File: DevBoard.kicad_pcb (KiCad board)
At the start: 2 copper layers, 100 x 100 mm, 116 parts, among them J1 Audio_In, J10 Jumper, J11 RJ45, J12 Jumper, J13 Jumper, J14 Jumper, J15 Jumper, J16 Jumper, J17 Jumper, J18 DAC_I2S, J19 DAC_OUT, J2 Audio_In, J20 DAC_Amplified, J21 DAC_Amplified, J22 Voltmeter_Power, J23 Voltmeter_Positive, J24 Voltmeter_Ground, J25 Conn_01x05_Pin, J26 Pot1, J27 Pot2, J28 Pot3, J29 Pot4, J3 Audio_Amplified, J30 CV_In, J31 Audio12V_In, J32 Audio_Scaled_Out, J33 CV_Scaled_Out, J4 Audio_Amplified, J5 CV_In, J6 CV_In, J7 CV_Amplified, J8 CV_Amplified, J9 Jumper, SW1 SW_DPST, U1 MCP6004, U2 TL074, U3 LM1117-3.3, U4 LM1117-5.0, U5 LM4040DBZ-5, U6 PCM5100APW, U8 TL072

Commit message: Started PCB layout
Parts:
- J11: moved to B.Cu
- moved R14 258.4 mm to (185.6, 105.4)
- moved R16 256.6 mm to (185.6, 101.4)
- moved R20 253.9 mm to (185.6, 107.4)
- moved R18 252.8 mm to (185.6, 95.4)
- moved R22 251.3 mm to (185.6, 97.4), turned to 180 degrees
- moved R24 250.5 mm to (185.6, 109.4)
- moved J3 247.0 mm to (185.4, 85.4), turned to -90 degrees
- moved R26 246.8 mm to (185.6, 93.4)
- moved R13 244.1 mm to (170.4, 105.4), turned to 180 degrees
- moved J4 243.1 mm to (185.4, 89.6), turned to -90 degrees
- moved R15 242.1 mm to (170.4, 101.4), turned to 180 degrees
- moved J1 241.6 mm to (170.6, 85.4), turned to 90 degrees
- moved R17 240.3 mm to (170.4, 95.4), turned to 180 degrees
- moved R19 239.6 mm to (170.4, 107.4), turned to 180 degrees
- moved J2 237.7 mm to (170.6, 89.6), turned to 90 degrees
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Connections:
- C6 pad 1: Net-(U2B-+) -> Net-(U2D-+)
- J1 pad 2: /Audio_In2 -> /Audio_Out1
- J2 pad 2: /Audio_In2 -> /Audio_Out1
- J3 pad 1: /Audio_Out1 -> /Audio_In2
- J30 pad 1: /CV_In2 -> /CV_In1
- J30 pad 2: /CV_In1 -> /CV_Scaled1
- J31 pad 2: /Audio12V_In2 -> /Audio_Scaled1
- J32 pad 1: /Audio_Scaled1 -> /Audio12V_In2
- J33 pad 1: /CV_Scaled1 -> /CV_In2
- J4 pad 1: /Audio_Out1 -> /Audio_In2
- J5 pad 2: /CV2_In -> /CV1_Out
- J6 pad 2: /CV2_In -> /CV1_Out
- J7 pad 1: /CV1_Out -> /CV2_In
- J8 pad 1: /CV1_Out -> /CV2_In
- R13 pad 1: Net-(U2C--) -> Net-(U2B--)
- R14 pad 1: Net-(U2D--) -> Net-(U2C--)
- R16 pad 1: Net-(U2B-+) -> Net-(U2D-+)
- R18 pad 1: Net-(U2B--) -> Net-(U2D--)
- R19 pad 2: Net-(U2C--) -> Net-(U2B--)
- R20 pad 2: Net-(U2D--) -> Net-(U2C--)
- R22 pad 2: Net-(U2B--) -> Net-(U2D--)
- U2 pad 10: /CV1_In -> /CV2_In
- U2 pad 12: /CV2_In -> Net-(U2D-+)
- U2 pad 14: Net-(R20-Pad1) -> Net-(R22-Pad1)
- U2 pad 5: Net-(U2B-+) -> /CV1_In
- U2 pad 7: Net-(R22-Pad1) -> Net-(R19-Pad1)
- U2 pad 8: Net-(R19-Pad1) -> Net-(R20-Pad1)
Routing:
- net /CV_Scaled2: track 5.94 -> 28.6 mm
- net /Audio_Scaled2: track 5.51 -> 26.8 mm
- net /CV1_In: track 0.00 -> 17.7 mm
- net /CV2_In: track 0.00 -> 17.4 mm
- net /Audio_In2: track 0.00 -> 16.7 mm
- net /Audio_In1: track 0.00 -> 16.7 mm
- net /Audio_Scaled1: track 5.59 -> 19.6 mm
- net Net-(R22-Pad1): track 0.00 -> 13.1 mm
- net /DAC_OUT_L: track 0.00 -> 13.0 mm
- net Net-(R21-Pad1): track 0.00 -> 12.8 mm
- net /Audio_Out2: track 0.00 -> 9.51 mm
- net /Audio_Out1: track 0.00 -> 9.51 mm
- net +12V: track 0.00 -> 9.40 mm
- net +3.3VA: track 0.00 -> 9.35 mm
- net Net-(U8B--): track 0.00 -> 8.65 mm
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
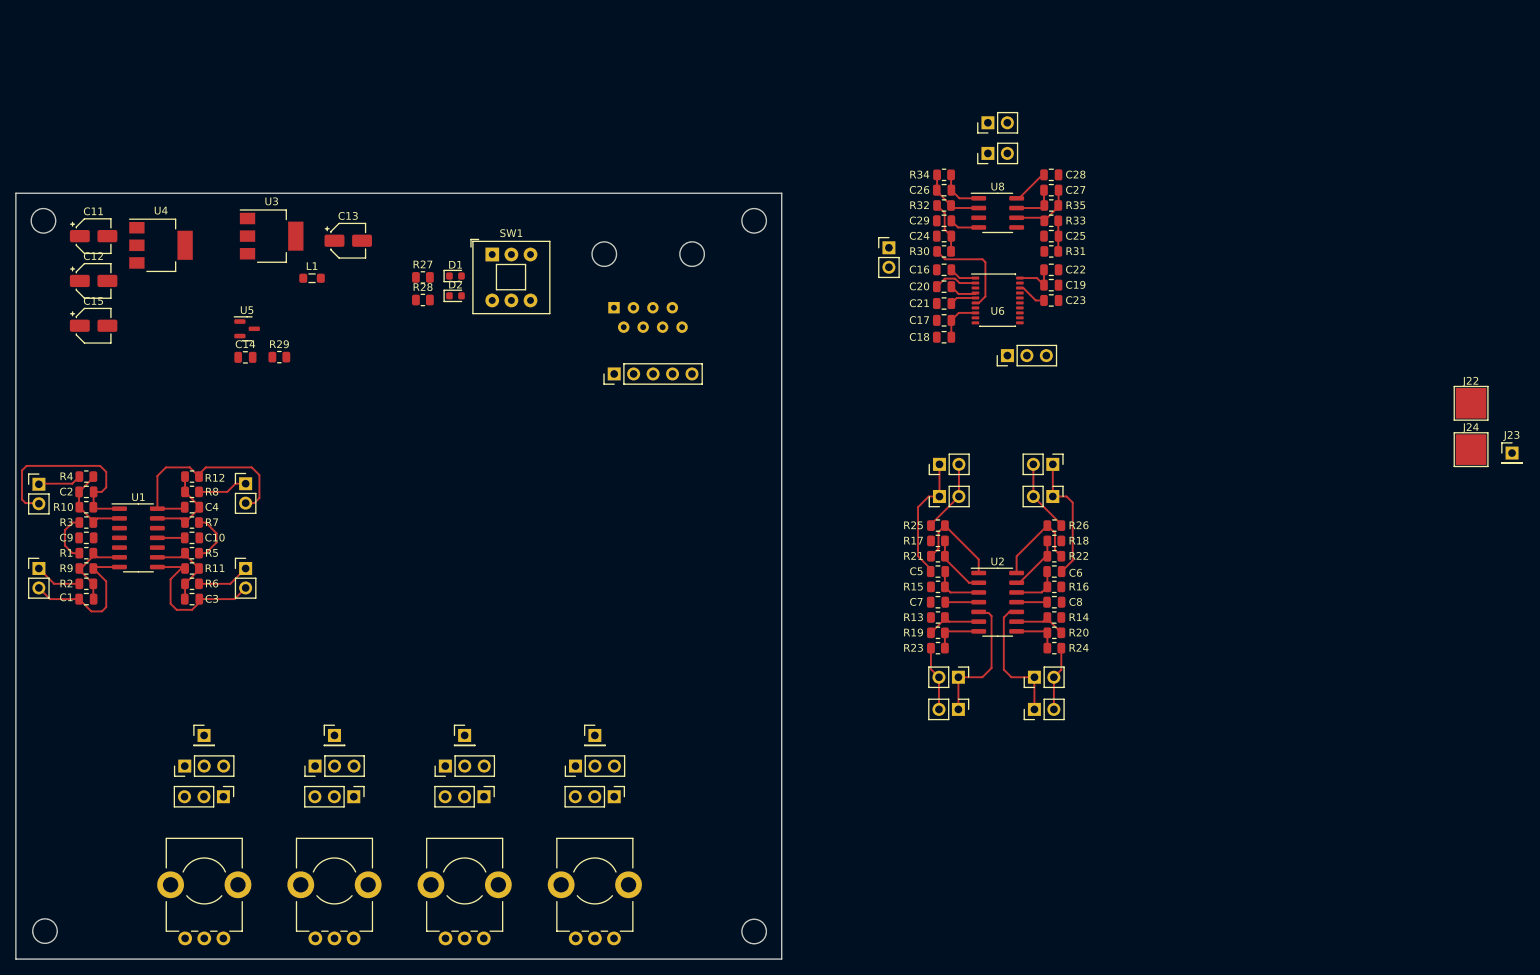
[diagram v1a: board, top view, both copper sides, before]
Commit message: Routing scaling circuits
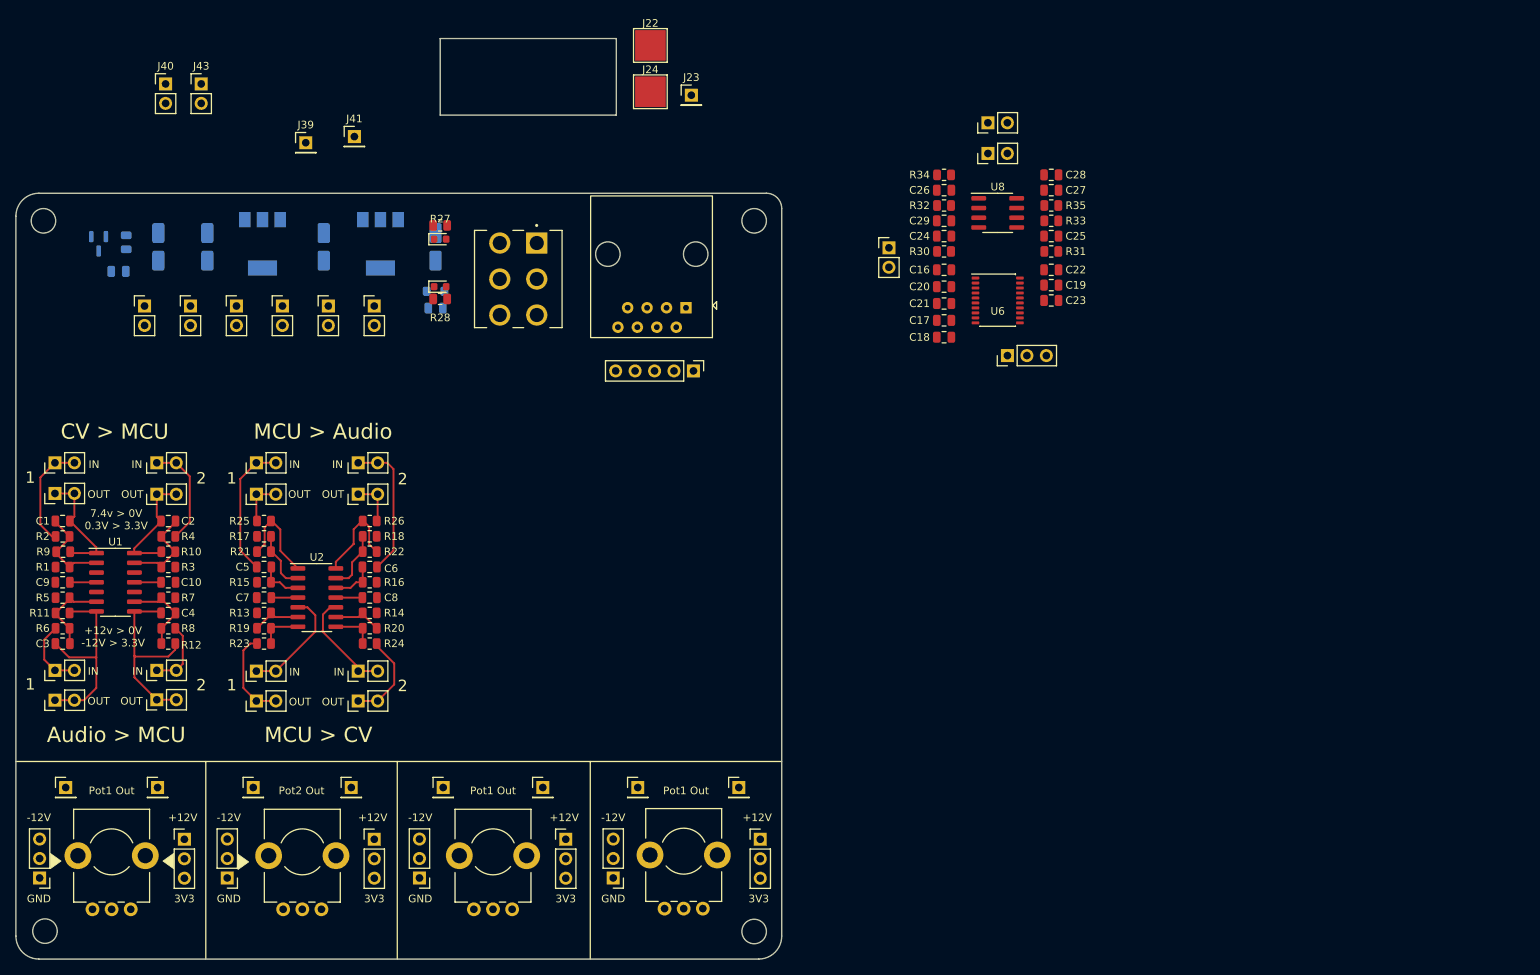
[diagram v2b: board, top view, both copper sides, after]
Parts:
- removed C15: 22uF, Capacitor_SMD:CP_Elec_4x5.8
- removed SW1: SW_DPST, Button_Switch_THT:SW_Push_2P2T_Toggle_CK_PVA2OAH5xxxxxxV2
- added C30: 47uF, Capacitor_SMD:CP_Elec_4x5.8, B.Cu at (90.2, 57.0)
- added C31: 22uF, Capacitor_SMD:CP_Elec_4x5.8, B.Cu at (68.6, 57.0)
- added J34: Power, Connector_PinHeader_2.54mm:PinHeader_1x02_P2.54mm_Vertical, F.Cu at (78.8, 64.7)
- added J35: Power, Connector_PinHeader_2.54mm:PinHeader_1x02_P2.54mm_Vertical, F.Cu at (72.8, 64.7)
- added J36: Power, Connector_PinHeader_2.54mm:PinHeader_1x02_P2.54mm_Vertical, F.Cu at (96.8, 64.7)
- added J37: Power, Connector_PinHeader_2.54mm:PinHeader_1x02_P2.54mm_Vertical, F.Cu at (90.8, 64.7)
- added J38: Power, Connector_PinHeader_2.54mm:PinHeader_1x02_P2.54mm_Vertical, F.Cu at (66.8, 64.7)
- added J39: Power_Test, Connector_PinHeader_2.54mm:PinHeader_1x01_P2.54mm_Vertical, F.Cu at (87.8, 43.4)
- added J40: Power, Connector_PinHeader_2.54mm:PinHeader_1x02_P2.54mm_Vertical, F.Cu at (69.5, 35.7)
- added J41: Power_Test, Connector_PinHeader_2.54mm:PinHeader_1x01_P2.54mm_Vertical, F.Cu at (94.2, 42.6)
- added J42: Power, Connector_PinHeader_2.54mm:PinHeader_1x02_P2.54mm_Vertical, F.Cu at (84.8, 64.7)
- added J43: Power, Connector_PinHeader_2.54mm:PinHeader_1x02_P2.54mm_Vertical, F.Cu at (74.2, 35.7)
- added J44: Pot1, Connector_PinHeader_2.54mm:PinHeader_1x01_P2.54mm_Vertical, F.Cu at (68.5, 127.6)
- added J45: Pot2, Connector_PinHeader_2.54mm:PinHeader_1x01_P2.54mm_Vertical, F.Cu at (93.8, 127.6)
- added J46: Pot3, Connector_PinHeader_2.54mm:PinHeader_1x01_P2.54mm_Vertical, F.Cu at (118.8, 127.6)
- added J47: Pot4, Connector_PinHeader_2.54mm:PinHeader_1x01_P2.54mm_Vertical, F.Cu at (144.4, 127.6)
- added J48: CV_In1, Connector_PinHeader_2.54mm:PinHeader_1x02_P2.54mm_Vertical, F.Cu at (55.1, 112.3)
- added J49: CV_Scaled_Out2, Connector_PinHeader_2.54mm:PinHeader_1x02_P2.54mm_Vertical, F.Cu at (68.4, 116.1)
- added J50: Audio12V_In, Connector_PinHeader_2.54mm:PinHeader_1x02_P2.54mm_Vertical, F.Cu at (55.1, 89.2)
- added J51: Audio_Scaled_Out, Connector_PinHeader_2.54mm:PinHeader_1x02_P2.54mm_Vertical, F.Cu at (68.4, 85.2)
- added SW2: SW_DPDT_x2, Custom_Footprints:100DP6T1B1M2QE_ON_ON_ON, F.Cu at (115.6, 61.2)
- C11, C12, C14, L1, R29, U3, U4, U5: moved to B.Cu
- C13: value 47uF -> 10uF; footprint Capacitor_SMD:CP_Elec_4x5.8 -> Capacitor_SMD:C_0805_2012Metric; moved to B.Cu
- J11: moved to F.Cu
- J30: value CV_In -> CV_Scaled_Out1
- J33: value CV_Scaled_Out -> CV_In2
- J6: value CV_In -> CV_Out
- moved J23 116.9 mm to (138.2, 37.2)
- moved J22 116.9 mm to (132.8, 30.7)
- moved J24 116.9 mm to (132.8, 36.8)
- moved J5 91.8 mm to (81.4, 112.4), turned to 90 degrees
- moved J6 91.7 mm to (81.4, 116.3), turned to 90 degrees
- moved J4 90.7 mm to (94.7, 89.3), turned to 90 degrees
- moved J3 90.7 mm to (94.7, 85.2), turned to 90 degrees
- moved C6 89.4 mm to (96.2, 98.8)
- moved C8 89.4 mm to (96.2, 102.8)
- moved R14 89.4 mm to (96.2, 104.8)
- moved R16 89.4 mm to (96.2, 100.8)
- moved R18 89.4 mm to (96.2, 94.8)
- moved R20 89.4 mm to (96.2, 106.8)
- moved R22 89.4 mm to (96.2, 96.8)
- moved R24 89.4 mm to (96.2, 108.8)
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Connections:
- C1 pad 2: Net-(U1B--) -> Net-(U1A--)
- C13 pad 1: +12V -> +3.3VA
- C14 pad 1: /AREF_-5 -> -5V
- C2 pad 2: Net-(U1A--) -> Net-(U1D--)
- C3 pad 1: /CV_Scaled1 -> /CV_Scaled_Out1
- C3 pad 2: Net-(U1C--) -> Net-(U1B--)
- C4 pad 1: /CV_Scaled2 -> /CV_Scaled_Out2
- C4 pad 2: Net-(U1D--) -> Net-(U1C--)
- J1 pad 2: /Audio_Out1 -> /Audio_In1
- J2 pad 1: /Audio_In1 -> /Audio_Out1
- J3 pad 2: /Audio_Out2 -> /Audio_In2
- J30 pad 1: /CV_In1 -> /CV_Scaled_Out1
- J30 pad 2: /CV_Scaled1 -> /CV_Scaled_Out1
- J31 pad 2: /Audio_Scaled1 -> /Audio12V_In1
- J32 pad 1: /Audio12V_In2 -> /Audio_Scaled2
- J33 pad 2: /CV_Scaled2 -> /CV_In2
- J4 pad 1: /Audio_In2 -> /Audio_Out2
- J5 pad 2: /CV1_Out -> /CV1_In
- J6 pad 1: /CV1_In -> /CV1_Out
- J7 pad 2: /CV2_Out -> /CV2_In
- J8 pad 1: /CV2_In -> /CV2_Out
- R1 pad 1: Net-(U1B--) -> Net-(U1A--)
- R1 pad 2: /-5V_REF -> -5V
- R10 pad 2: Net-(U1A--) -> Net-(U1D--)
- R11 pad 1: /CV_Scaled1 -> /CV_Scaled_Out1
- R11 pad 2: Net-(U1C--) -> Net-(U1B--)
- R12 pad 1: /CV_Scaled2 -> /CV_Scaled_Out2
- R12 pad 2: Net-(U1D--) -> Net-(U1C--)
- R2 pad 1: Net-(U1B--) -> Net-(U1A--)
- R29 pad 2: /AREF_-5 -> -5V
- R3 pad 1: Net-(U1A--) -> Net-(U1D--)
- R3 pad 2: /-5V_REF -> -5V
- R4 pad 1: Net-(U1A--) -> Net-(U1D--)
- R5 pad 1: Net-(U1C--) -> Net-(U1B--)
- R5 pad 2: /-5V_REF -> -5V
- R6 pad 1: Net-(U1C--) -> Net-(U1B--)
- R7 pad 1: Net-(U1D--) -> Net-(U1C--)
- R7 pad 2: /-5V_REF -> -5V
- R8 pad 1: Net-(U1D--) -> Net-(U1C--)
- R9 pad 2: Net-(U1B--) -> Net-(U1A--)
- U1 pad 1: /Audio_Scaled2 -> /Audio_Scaled1
- U1 pad 14: /CV_Scaled2 -> /Audio_Scaled2
- U1 pad 7: /Audio_Scaled1 -> /CV_Scaled_Out1
- U1 pad 8: /CV_Scaled1 -> /CV_Scaled_Out2
- U5 pad 2: /AREF_-5 -> -5V
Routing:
- net /CV_Scaled2: track 28.6 -> 0.00 mm
- net /CV_Scaled_Out1: track 0.00 -> 25.6 mm
- net /CV_Scaled_Out2: track 0.00 -> 25.5 mm
- net /CV_Scaled1: track 20.7 -> 0.00 mm
- net /-5V_REF: track 13.5 -> 0.00 mm
- net /DAC_OUT_L: track 13.0 -> 0.00 mm
- net /Audio_Scaled2: track 26.8 -> 15.6 mm
- net +3.3VA: track 9.35 -> 0.00 mm
- net Net-(U8B--): track 8.65 -> 0.00 mm
- net Net-(U8A--): track 8.44 -> 0.00 mm
- net /Audio12V_In1: track 6.31 -> 14.0 mm
- net /Audio12V_In2: track 6.07 -> 13.7 mm
- net Net-(C24-Pad1): track 6.79 -> 0.00 mm
- net /DAC_OUT_AMP_L: track 5.93 -> 0.00 mm
- net /DAC_OUT_AMP_R: track 5.86 -> 0.00 mm
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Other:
- board size 100 x 100 mm -> 100 x 120.2 mm
- board text added: "+12V"
- board text added: "+12v > 0V -12V > 3.3V"
- board text added: "-12V"
- board text added: "1"
- board text added: "2"
- board text added: "3V3"
- board text added: "7.4v > 0V 0.3V > 3.3V"
- board text added: "Audio > MCU"
- board text added: "CV > MCU"
- board text added: "GND"
- board text added: "IN"
- board text added: "MCU > Audio"
- board text added: "MCU > CV"
- board text added: "OUT"
- board text added: "Pot1 Out"
- board text added: "Pot2 Out"

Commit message: Further layout
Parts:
- removed C10: 1uF, Capacitor_SMD:C_0805_2012Metric
- added D3: 5V_LED, LED_SMD:LED_0603_1608Metric, F.Cu at (121.7, 61.9)
- added D4: 3V3_LED, LED_SMD:LED_0603_1608Metric, F.Cu at (121.7, 64.2)
- added R36: 2k2, Resistor_SMD:R_0805_2012Metric, F.Cu at (118.3, 61.9)
- added R37: 2k2, Resistor_SMD:R_0805_2012Metric, F.Cu at (118.3, 64.2)
- D1: value LED_Small -> 12V_LED
- D2: value LED_Small -> -12V_LED
- moved J18 122.0 mm to (57.5, 72.8), turned to 180 degrees
- moved C23 121.1 mm to (64.2, 70.0), turned to 90 degrees
- moved C19 119.3 mm to (66.2, 70.0), turned to -90 degrees
- moved C22 117.4 mm to (68.2, 70.0), turned to -90 degrees
- moved R31 115.3 mm to (70.6, 70.0), turned to 90 degrees
- moved U6 114.0 mm to (64.2, 63.1), turned to -90 degrees
- moved C25 113.5 mm to (72.6, 70.0), turned to 90 degrees
- moved C18 112.2 mm to (59.7, 56.1), turned to 90 degrees
- moved R33 111.8 mm to (74.6, 70.0), turned to -90 degrees
- moved C28 110.9 mm to (76.6, 70.0), turned to 90 degrees
- moved C31 110.4 mm to (178.8, 51.2)
- moved U3 110.4 mm to (207.8, 50.8)
- moved C11 110.4 mm to (215.0, 51.2)
- moved C13 110.4 mm to (215.0, 59.2)
- moved C30 110.4 mm to (200.4, 51.2)
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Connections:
- C9 pad 2: +12V -> +3.3VA
- J20 pad 2: /DAC_OUT_AMP_R -> /DAC_OUT_AMP_L
- J21 pad 1: /DAC_OUT_AMP_L -> /DAC_OUT_AMP_R
- U1 pad 11: -12V -> GND
- U1 pad 4: +12V -> +3.3VA
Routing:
- net /DAC_OUT_L: track 0.00 -> 32.9 mm
- net /DAC_OUT_AMP_R: track 0.00 -> 29.8 mm
- net /DAC_OUT_R: track 0.00 -> 19.1 mm
- net /DAC_OUT_AMP_L: track 0.00 -> 14.9 mm
- net +3.3VA: track 0.00 -> 12.5 mm
- net Net-(U8B--): track 0.00 -> 10.7 mm
- net /DAC_LRCLK: track 0.00 -> 9.91 mm
- net Net-(U8A--): track 0.00 -> 8.45 mm
- net /DAC_DATA: track 0.00 -> 8.00 mm
- net Net-(C24-Pad1): track 0.00 -> 6.79 mm
- net /DAC_BCLK: track 0.00 -> 6.15 mm
- net Net-(U6-CAPP): track 0.00 -> 5.74 mm
- net +3V3: track 0.00 -> 5.42 mm
- net Net-(C25-Pad1): track 0.00 -> 4.03 mm
- net Net-(U6-LDOO): track 0.00 -> 3.71 mm
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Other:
- board text added: "5V"
- board text added: "Bit Clk"
- board text added: "DAC"
- board text added: "Data"
- board text added: "L"
- board text added: "LR Clk"
- board text added: "OFF"
- board text added: "ON"
- board text added: "Out Amp"
- board text added: "Out L"
- board text added: "Out R"
- board text added: "R"

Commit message: PCB Updates
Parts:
- added REF**: MountingHole_2.5mm, MountingHole:MountingHole_2.5mm, F.Cu at (108.2, 118.7)
- added REF**: MountingHole_2.5mm, MountingHole:MountingHole_2.5mm, F.Cu at (133.8, 118.6)
- J22, J24: moved to B.Cu
- moved C18 119.5 mm to (140.7, 143.9), turned to -90 degrees
- moved C17 116.6 mm to (138.6, 143.9), turned to -90 degrees
- moved J19 116.3 mm to (142.9, 139.5), turned to 180 degrees
- moved C21 113.9 mm to (136.5, 143.9), turned to -90 degrees
- moved C20 111.3 mm to (134.4, 143.9), turned to 90 degrees
- moved C16 108.8 mm to (132.3, 143.9), turned to -90 degrees
- moved R30 105.7 mm to (129.8, 143.8), turned to -90 degrees
- moved C24 103.5 mm to (127.8, 143.8), turned to -90 degrees
- moved U6 103.2 mm to (136.2, 136.9), turned to 90 degrees
- moved C29 101.5 mm to (125.8, 143.8), turned to 90 degrees
- moved J18 101.2 mm to (142.9, 127.2), turned to 0 degrees
- moved R32 99.5 mm to (123.8, 143.8), turned to -90 degrees
- moved J22 97.8 mm to (113.8, 126.6), turned to 90 degrees
- moved C26 97.7 mm to (121.8, 143.8), turned to -90 degrees
- moved J20 97.6 mm to (114.0, 146.8), turned to 180 degrees
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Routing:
- net GND: track 3.58 -> 0.00 mm
- net /DAC_OUT_AMP_R: track 29.8 -> 29.2 mm
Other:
- board size 100 x 120.2 mm -> 100 x 100 mm
- board text added: "+12v > 0v -12v > 3.3v"
- board text added: "0v > -7.8v 3.3v > 7.8v"
- board text added: "0v > 0v 3.3v > 8v"
- board text added: "3"
- board text added: "4"
- board text added: "7.4v > 0v 0.3v > 3.3v"
- board text added: "Ext In"
- board text added: "Out"
- board text added: "Pot 1"
- board text added: "Pot 2"
- board text added: "Pot 3"
- board text added: "Pot 4"
- board text added: "Pot Out"
- board text added: "Voltmeter IN"
- board text removed: "+12v > 0V -12V > 3.3V"
- board text removed: "7.4v > 0V 0.3V > 3.3V"
- board text removed: "OFF"
- board text removed: "Pot1 Out"
- board text removed: "Pot2 Out"
